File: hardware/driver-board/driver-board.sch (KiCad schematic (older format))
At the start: 0 parts

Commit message: Add display schematics
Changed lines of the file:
@@
 $Descr A4 11693 8268
 encoding utf-8
-Sheet 1 6
+Sheet 1 7
 Title "FT81x TFT040 Driver Board"
-Date "2020-07-03"
+Date "2020-07-05"
 Rev "2007D"
 Comp ""
@@
 F1 "ft81x.sch" 50
 $EndSheet
+$Sheet
+S 3300 4250 500  150
+U 5F096907
+F0 "Display" 50
+F1 "display.sch" 50
+$EndSheet
 $EndSCHEMATC

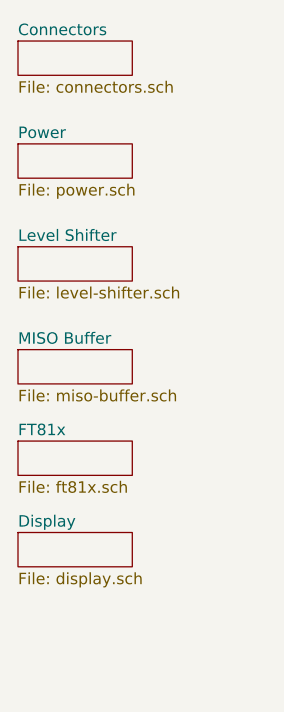
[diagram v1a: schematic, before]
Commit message: Add testpoints
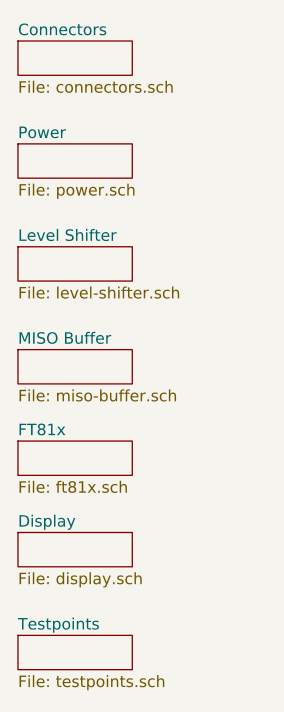
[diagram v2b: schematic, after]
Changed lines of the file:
@@
 $Descr A4 11693 8268
 encoding utf-8
-Sheet 1 7
+Sheet 1 8
 Title "FT81x TFT040 Driver Board"
-Date "2020-07-05"
+Date "2020-07-06"
 Rev "2007D"
 Comp ""
@@
 F1 "display.sch" 50
 $EndSheet
+$Sheet
+S 3300 4700 500  150
+U 5F0302AD
+F0 "Testpoints" 50
+F1 "testpoints.sch" 50
+$EndSheet
 $EndSCHEMATC
